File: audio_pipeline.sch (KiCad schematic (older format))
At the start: 13 parts, among them U1 MAX4582, U2 DS1882

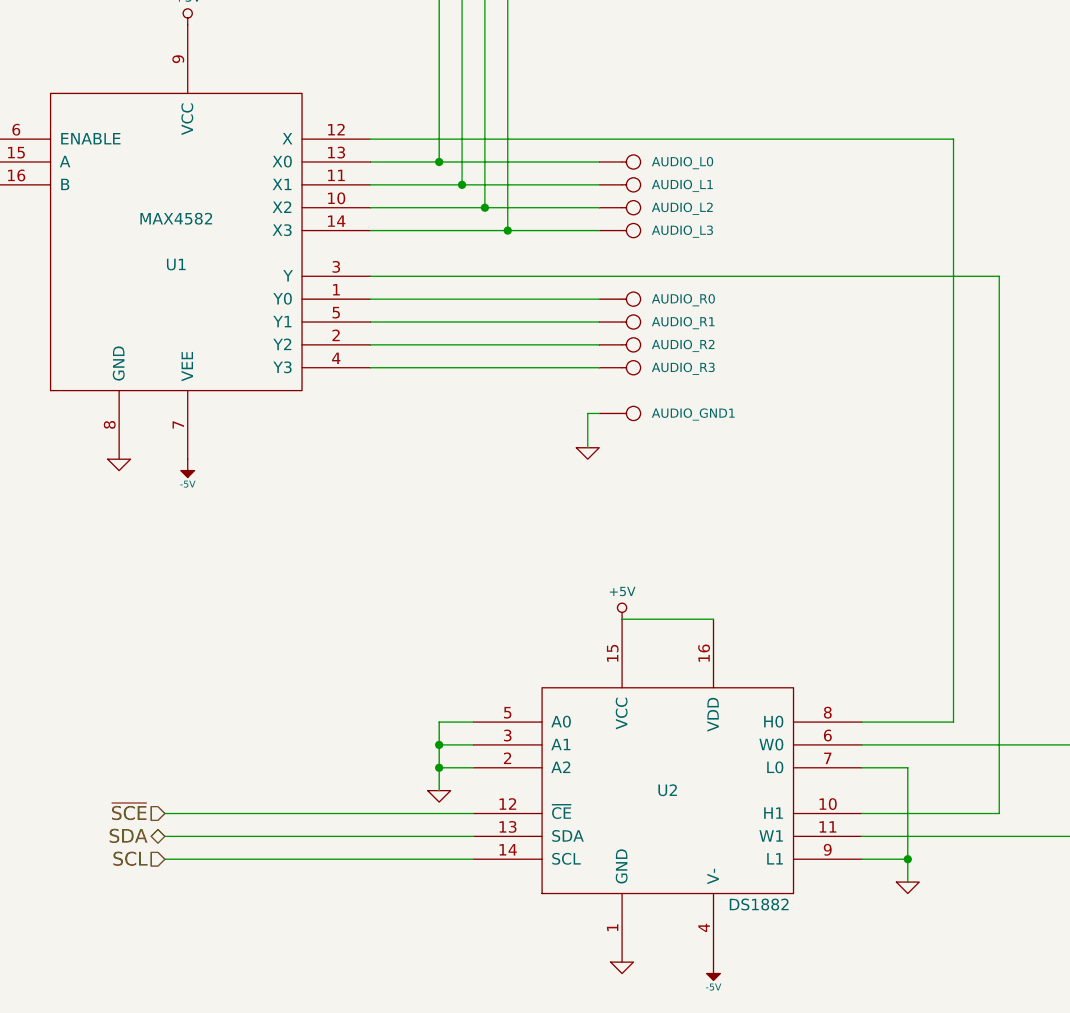
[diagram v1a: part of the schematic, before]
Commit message: First experiments with board layout, plus modules for the AC/DC power unit and LCD.
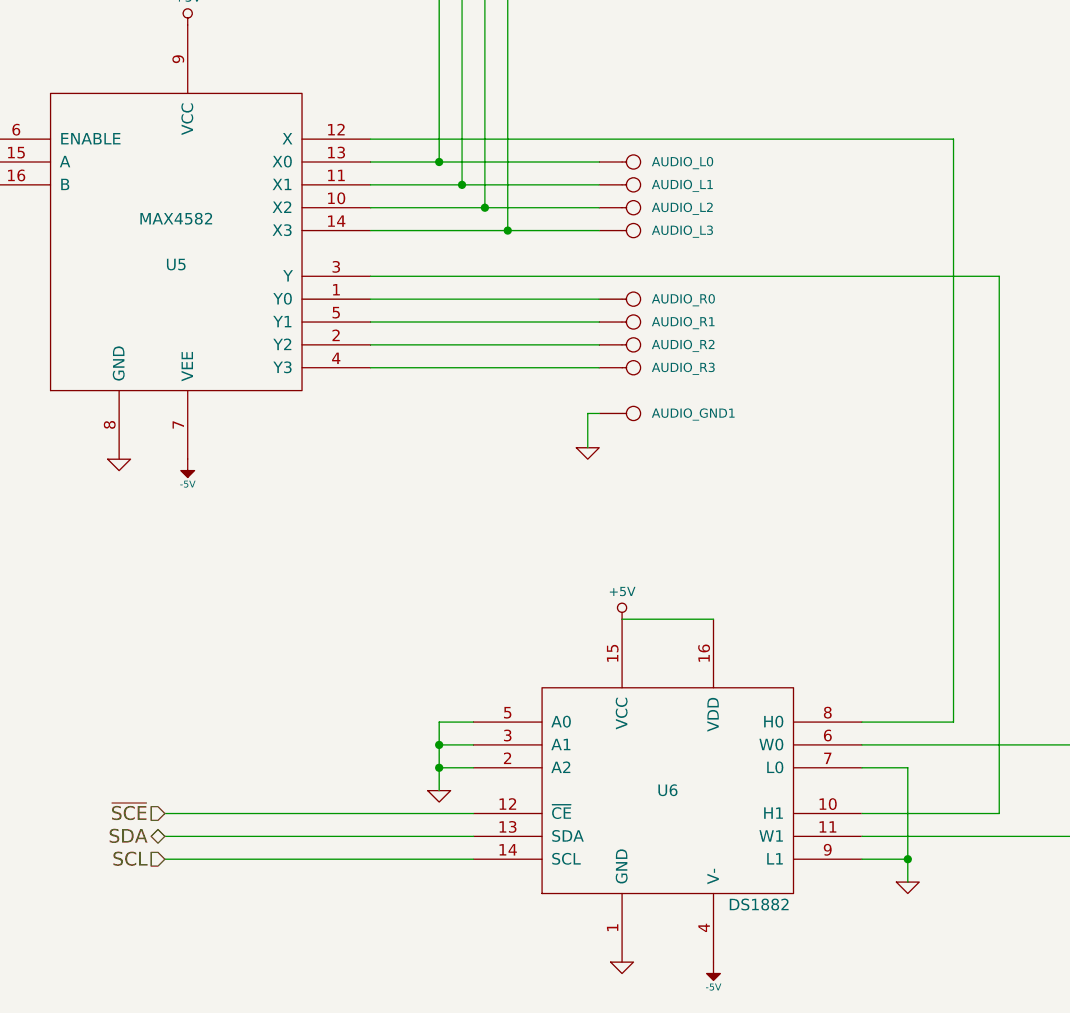
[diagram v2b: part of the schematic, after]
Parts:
- renumbered U1 to U5, U2 to U6
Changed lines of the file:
@@
-EESchema Schematic File Version 2  date Saturday, June 02, 2012 10:08:47 pm
+EESchema Schematic File Version 2  date 6/14/2012 10:22:20 PM
 LIBS:atmel
 LIBS:device
@@
 LIBS:BP5037
 LIBS:MCP23017
-LIBS:hdsp
 LIBS:lumex
+LIBS:dual_mos_p
 LIBS:kenwood-cache
 EELAYER 25  0
@@
 Sheet 3 3
 Title ""
-Date "3 jun 2012"
+Date "10 jun 2012"
 Rev ""
 Comp ""
@@
 	4800 3500 5800 3500
 Wire Wire Line
-	5800 3100 5300 3100
-Wire Wire Line
-	5300 3100 4800 3100
-Wire Wire Line
-	5800 2900 5100 2900
-Wire Wire Line
-	5100 2900 4800 2900
+	5800 3100 4800 3100
+Wire Wire Line
+	5800 2900 4800 2900
 Connection ~ 5100 5550
 Wire Wire Line
-	5100 5550 5250 5550
-Wire Wire Line
-	5100 5650 5100 5550
-Wire Wire Line
-	5100 5550 5100 5450
-Wire Wire Line
-	5100 5450 5100 5350
+	5250 5550 5100 5550
+Wire Wire Line
+	5100 5650 5100 5350
 Wire Wire Line
 	5100 5350 5250 5350
@@
 Connection ~ 7150 5950
 Wire Wire Line
-	7150 6050 7150 5950
-Wire Wire Line
-	7150 5950 7150 5550
+	7150 6050 7150 5550
 Wire Wire Line
 	7150 5550 6950 5550
@@
 Connection ~ 5100 5450
 Wire Wire Line
-	5800 3000 5200 3000
-Wire Wire Line
-	5200 3000 4800 3000
-Wire Wire Line
-	5800 3200 5400 3200
-Wire Wire Line
-	5400 3200 4800 3200
+	5800 3000 4800 3000
+Wire Wire Line
+	5800 3200 4800 3200
 Wire Wire Line
 	5800 3600 4800 3600
@@
 AUDIO3_MONITOR
 $Comp
-L GND #PWR5
+L GND #PWR042
 U 1 1 4F8F6783
 P 5750 4150
-F 0 "#PWR5" H 5750 4150 30  0001 C CNN
+F 0 "#PWR042" H 5750 4150 30  0001 C CNN
 F 1 "GND" H 5750 4080 30  0001 C CNN
 	1    5750 4150
@@
 SDA
 $Comp
-L MAX4582 U1
+L MAX4582 U5
 U 1 1 4F88F500
 P 3950 3250
-F 0 "U1" H 3950 3150 50  0000 C CNN
+F 0 "U5" H 3950 3150 50  0000 C CNN
 F 1 "MAX4582" H 3950 3350 50  0000 C CNN
 F 2 "MODULE" H 3950 3250 50  0001 C CNN
@@
 $EndComp
 $Comp
-L -5V #PWR8
+L -5V #PWR043
 U 1 1 4F8E0C7B
 P 6300 6400
-F 0 "#PWR8" H 6300 6540 20  0001 C CNN
+F 0 "#PWR043" H 6300 6540 20  0001 C CNN
 F 1 "-5V" H 6300 6510 30  0000 C CNN
 	1    6300 6400
@@
 $EndComp
 $Comp
-L +5V #PWR6
+L +5V #PWR044
 U 1 1 4F8E0C5D
 P 5900 4900
-F 0 "#PWR6" H 5900 5050 40  0001 C CNN
+F 0 "#PWR044" H 5900 5050 40  0001 C CNN
 F 1 "+5V" H 5900 5020 40  0000 C CNN
 	1    5900 4900
@@
 $EndComp
 $Comp
-L GND #PWR7
+L GND #PWR045
 U 1 1 4F8E0C4F
 P 5900 6400
-F 0 "#PWR7" H 5900 6400 30  0001 C CNN
+F 0 "#PWR045" H 5900 6400 30  0001 C CNN
 F 1 "GND" H 5900 6330 30  0001 C CNN
 	1    5900 6400
@@
 $EndComp
 $Comp
-L GND #PWR4
+L GND #PWR046
 U 1 1 4F8E0C00
 P 5100 5650
-F 0 "#PWR4" H 5100 5650 30  0001 C CNN
+F 0 "#PWR046" H 5100 5650 30  0001 C CNN
 F 1 "GND" H 5100 5580 30  0001 C CNN
 	1    5100 5650
@@
 $EndComp
 $Comp
-L DS1882 U2
+L DS1882 U6
 U 1 1 4F8E0BE3
 P 6100 5650
-F 0 "U2" H 6100 5650 50  0000 C CNN
+F 0 "U6" H 6100 5650 50  0000 C CNN
 F 1 "DS1882" H 6500 5150 50  0000 C CNN
 F 2 "SOIC16" H 5700 5150 50  0001 C CNN
@@
 $EndComp
 $Comp
-L GND #PWR9
+L GND #PWR047
 U 1 1 4F896654
 P 7150 6050
-F 0 "#PWR9" H 7150 6050 30  0001 C CNN
+F 0 "#PWR047" H 7150 6050 30  0001 C CNN
 F 1 "GND" H 7150 5980 30  0001 C CNN
 	1    7150 6050
@@
 $EndComp
 $Comp
-L +5V #PWR2
+L +5V #PWR048
 U 1 1 4F88F637
 P 4000 2300
-F 0 "#PWR2" H 4000 2450 40  0001 C CNN
+F 0 "#PWR048" H 4000 2450 40  0001 C CNN
 F 1 "+5V" H 4000 2420 40  0000 C CNN
 	1    4000 2300
@@
 $EndComp
 $Comp
-L -5V #PWR3
+L -5V #PWR049
 U 1 1 4F88F61F
 P 4000 4200
-F 0 "#PWR3" H 4000 4340 20  0001 C CNN
+F 0 "#PWR049" H 4000 4340 20  0001 C CNN
 F 1 "-5V" H 4000 4310 30  0000 C CNN
 	1    4000 4200
@@
 $EndComp
 $Comp
-L GND #PWR1
+L GND #PWR050
 U 1 1 4F88F5F7
 P 3700 4200
-F 0 "#PWR1" H 3700 4200 30  0001 C CNN
+F 0 "#PWR050" H 3700 4200 30  0001 C CNN
 F 1 "GND" H 3700 4130 30  0001 C CNN
 	1    3700 4200

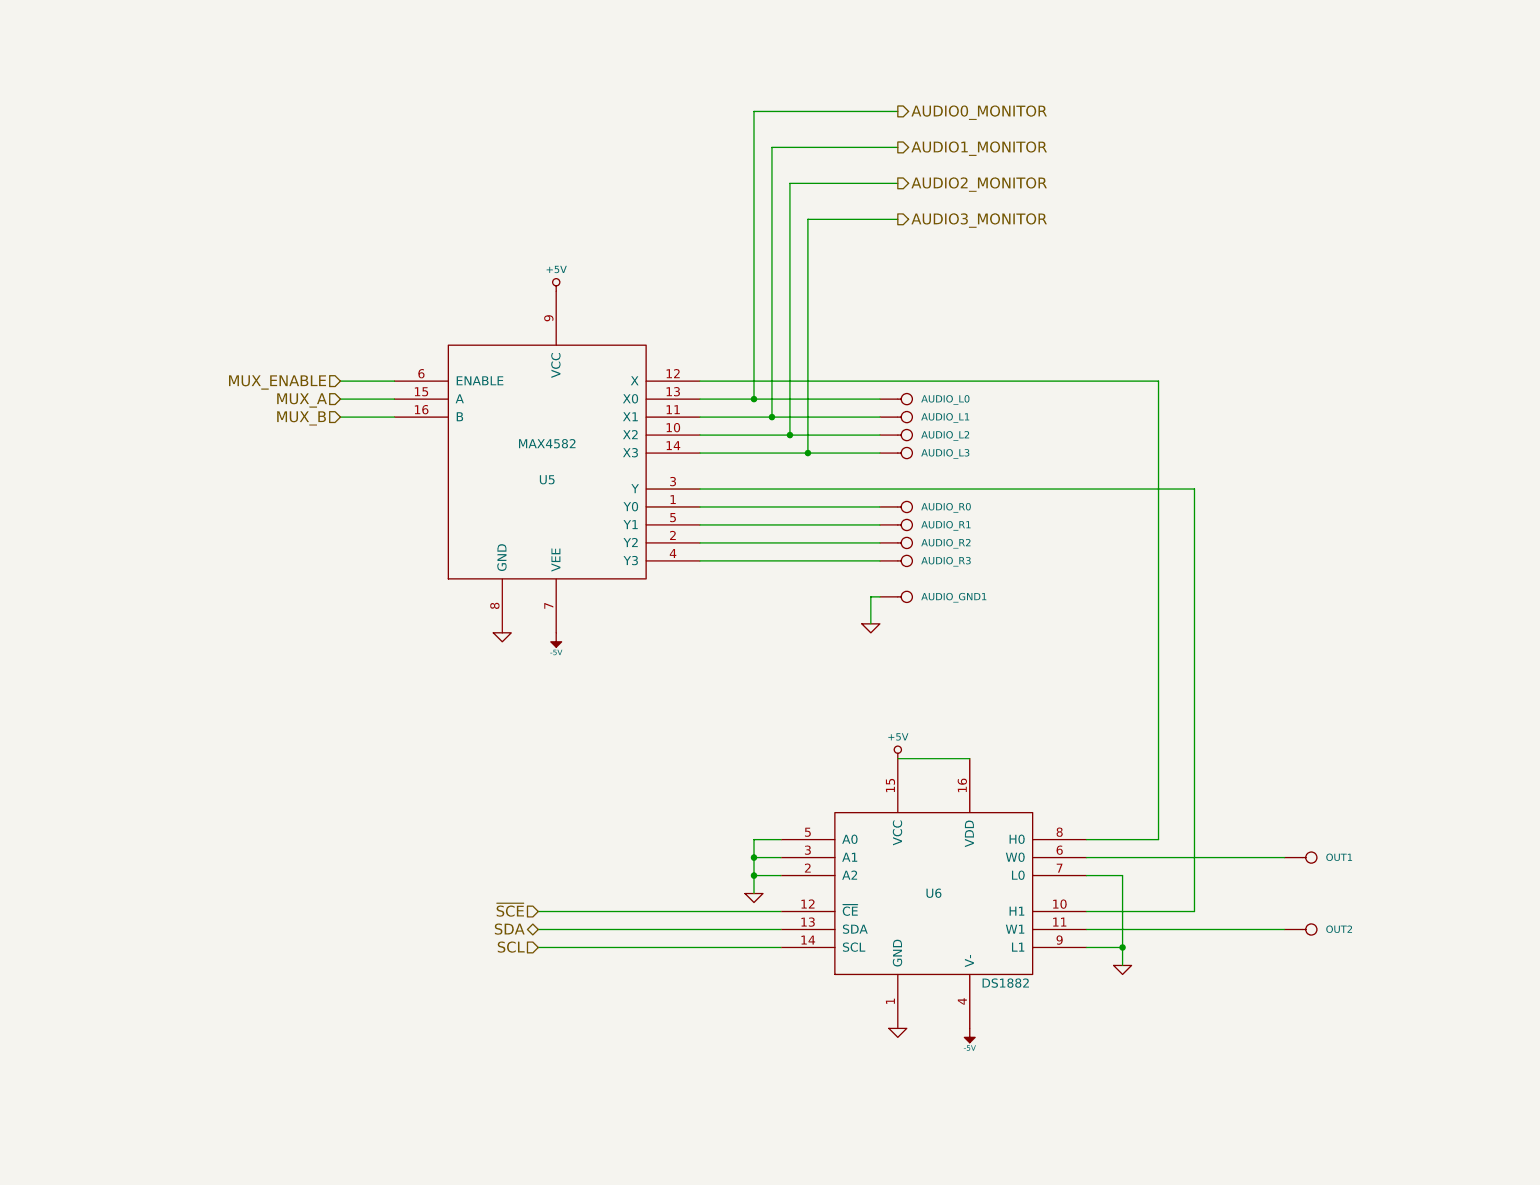
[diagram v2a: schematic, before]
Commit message: Adding back library files in same repo.
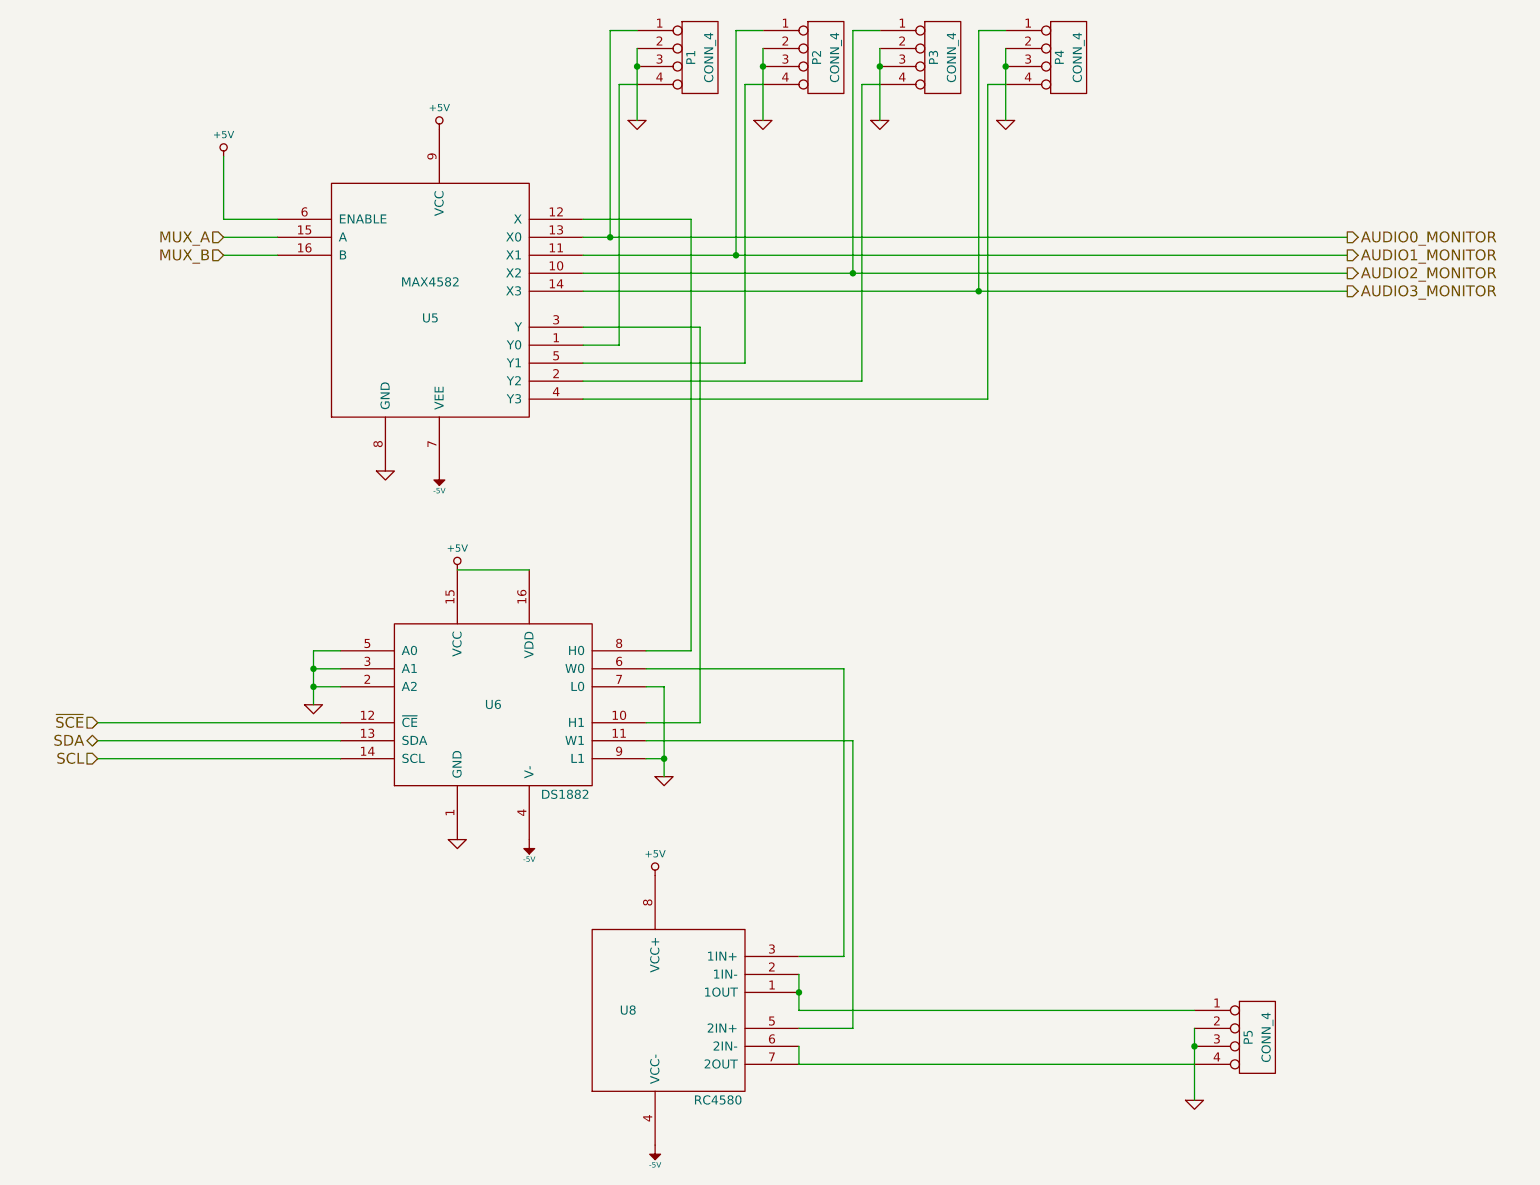
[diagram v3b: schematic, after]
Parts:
- removed AUDIO_GND1, AUDIO_L0, AUDIO_L1, AUDIO_L2, AUDIO_L3, AUDIO_R0, AUDIO_R1, AUDIO_R2, AUDIO_R3, OUT1, OUT2: CONN_1, symbol CONN_1
- added P1, P2, P3, P4, P5: CONN_4, symbol CONN_4
- added U8: RC4580, MODULE, symbol RC4580
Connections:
- net MUX_ENABLE is gone; now on net +5V: U5.6 (ENABLE)
- net +5V: now also U8.8 (VCC+)
- net -5V: now also U8.4 (VCC-)
- net AUDIO0_MONITOR: now also P1.1 (P1)
- net AUDIO1_MONITOR: now also P2.1 (P1)
- net AUDIO2_MONITOR: now also P3.1 (P1)
- net AUDIO3_MONITOR: now also P4.1 (P1)
- net GND: now also P1.2 (P2), P1.3 (P3), P2.2 (P2), P2.3 (P3), P3.2 (P2), P3.3 (P3), P4.2 (P2), P4.3 (P3), P5.2 (P2), P5.3 (P3)
- net at U5.1 (Y0): now also P1.4 (P4)
- net at U5.2 (Y2): now also P3.4 (P4)
- net at U5.4 (Y3): now also P4.4 (P4)
- net at U5.5 (Y1): now also P2.4 (P4)
- net at U6.6 (W0): now also U8.3 (1IN+)
- net at U6.11 (W1): now also U8.5 (2IN+)
- new net: P5.1 (P1), U8.1 (1OUT), U8.2 (1IN-)
- new net: P5.4 (P4), U8.6 (2IN-), U8.7 (2OUT)
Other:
- moved on the sheet: U5, U6
